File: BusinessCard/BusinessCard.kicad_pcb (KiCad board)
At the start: 2 copper layers, 4 parts

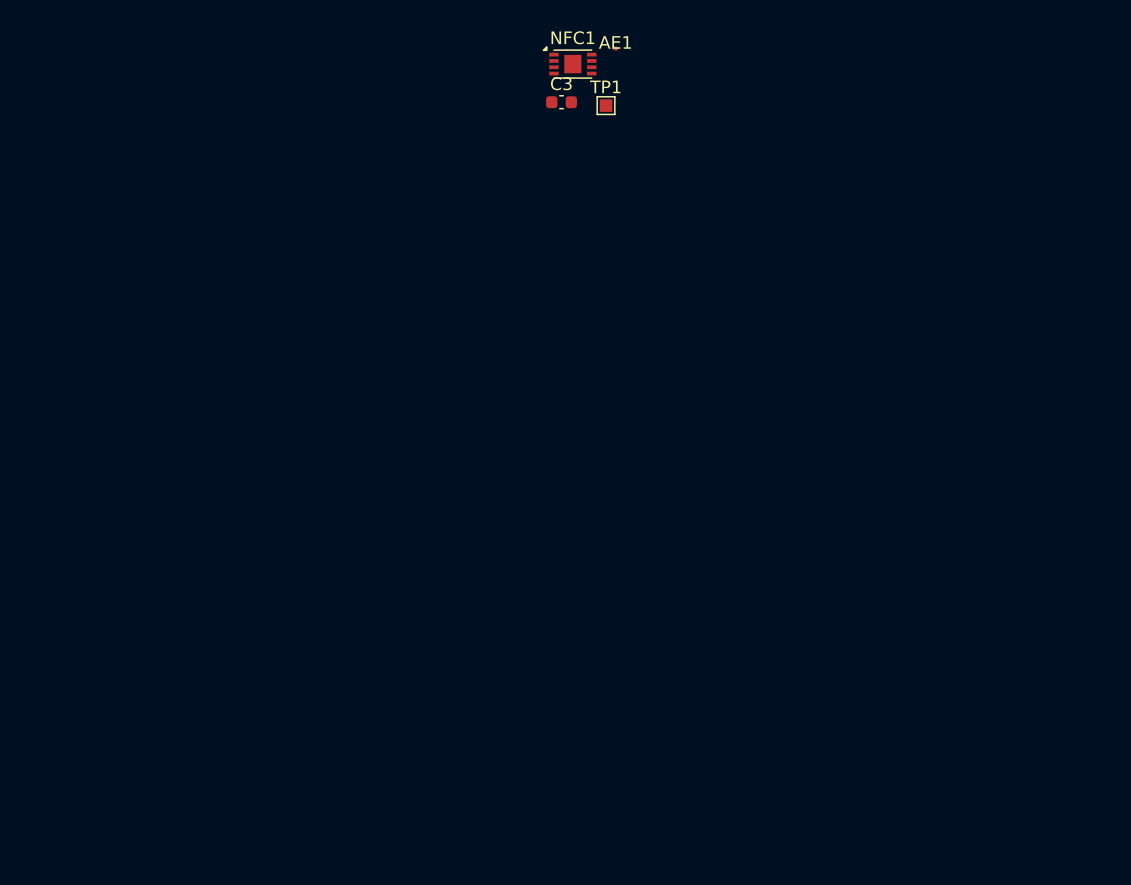
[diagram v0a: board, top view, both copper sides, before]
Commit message: Finished pcb circuit, added images
changed board color
rounded edges on board
redid trace sizing and width
rounded traces
silkscreen images added in
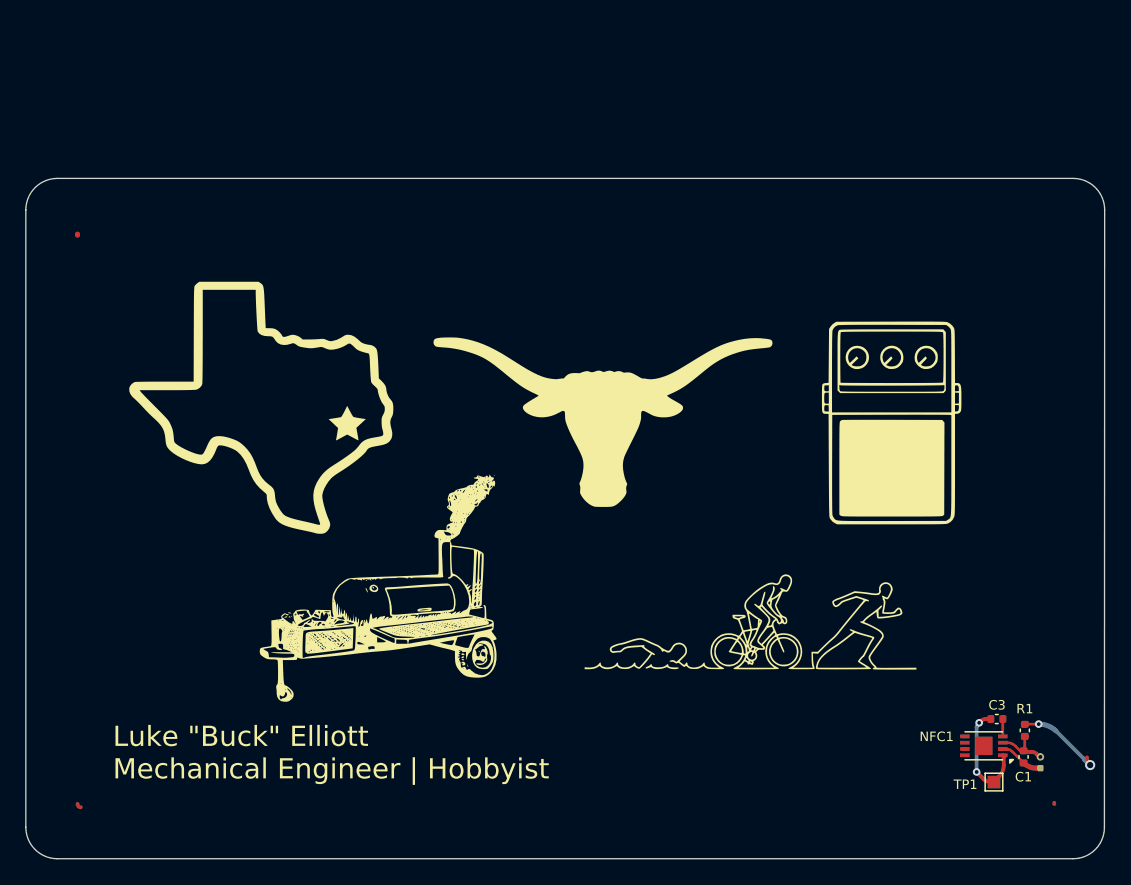
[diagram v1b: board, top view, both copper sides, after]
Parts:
- added C1: 18pF, Capacitor_SMD:C_0402_1005Metric, F.Cu at (179.2, 145.9)
- added G***: LOGO, bbq_pit, F.Cu at (128.0, 132.4)
- added G***: LOGO, guitar_pedal, F.Cu at (168.7, 119.4)
- added G***: LOGO, longhorn, F.Cu at (145.9, 119.0)
- added G***: LOGO, texas_image, F.Cu at (119.0, 117.9)
- added G***: LOGO, triathlon, F.Cu at (157.5, 131.1)
- added R1: 0, Capacitor_SMD:C_0402_1005Metric, F.Cu at (179.3, 143.8)
- C3: footprint Capacitor_SMD:C_0603_1608Metric -> Capacitor_SMD:C_0402_1005Metric
- moved AE1 66.1 mm to (180.8, 146.4), turned to 90 degrees
- moved NFC1 63.2 mm to (176.0, 145.0), turned to 180 degrees
- moved TP1 61.9 mm to (176.8, 147.9), turned to -90 degrees
- moved C3 59.9 mm to (177.0, 142.9), turned to 180 degrees
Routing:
- net Net-(NFC1-AC0): track 0.00 -> 1031.9 mm, vias 0 -> 2
- net Net-(NFC1-V_EH): track 0.00 -> 9.26 mm, vias 0 -> 2
- net Net-(NFC1-AC1): track 0.00 -> 4.39 mm
- net GND: track 0.00 -> 1.38 mm
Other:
- board outline added: 85.6 x 54 mm
- board text added: "Luke {dblquote}Buck{dblquote} Elliott Mechanical Engineer | Hobbyist"
